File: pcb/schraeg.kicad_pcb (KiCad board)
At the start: 2 copper layers, 39.5 x 110 mm, 99 parts, among them J1 PJ398SM, J2 PJ398SM, J3 PJ398SM, J4 PJ398SM, J5 PJ398SM, J6 PJ398SM, J7 PJ398SM, J8 POWER, SW1 CS12ANW03, SW2 CS12ANW03, SW3 CS12ANW03, U1 TL074, U2 TL074, U3 V2164, U4 TL074, U5 TL074

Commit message: Panel design on kicad and iBOM updated.
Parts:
- added G***: LOGO, schraeg:silkF, F.Cu at (76.0, 105.0)
- added G***: LOGO, schraeg:copperF, F.Cu at (76.0, 105.0)
- added G***: LOGO, schraeg:maskF, F.Cu at (76.0, 105.0)
- added REF**: MountingHole_3.2mm_M3, MountingHole:MountingHole_3.2mm_M3, F.Cu at (99.5, 145.5)
- added REF**: MountingHole_3.2mm_M3, MountingHole:MountingHole_3.2mm_M3, F.Cu at (96.8, 145.5)
- added REF**: MountingHole_3.2mm_M3, MountingHole:MountingHole_3.2mm_M3, F.Cu at (99.5, 64.5)
- added REF**: MountingHole_3.2mm_M3, MountingHole:MountingHole_3.2mm_M3, F.Cu at (99.5, 63.5)
- added REF**: MountingHole_3.2mm_M3, MountingHole:MountingHole_3.2mm_M3, F.Cu at (99.5, 62.5)
- added REF**: MountingHole_3.2mm_M3, MountingHole:MountingHole_3.2mm_M3, F.Cu at (99.5, 61.5)
- added REF**: MountingHole_3.2mm_M3, MountingHole:MountingHole_3.2mm_M3, F.Cu at (99.5, 60.5)
- added REF**: MountingHole_3.2mm_M3, MountingHole:MountingHole_3.2mm_M3, F.Cu at (96.8, 64.5)
- added REF**: MountingHole_3.2mm_M3, MountingHole:MountingHole_3.2mm_M3, F.Cu at (96.8, 63.5)
- added REF**: MountingHole_3.2mm_M3, MountingHole:MountingHole_3.2mm_M3, F.Cu at (96.8, 62.5)
- added REF**: MountingHole_3.2mm_M3, MountingHole:MountingHole_3.2mm_M3, F.Cu at (96.8, 61.5)
- added REF**: MountingHole_3.2mm_M3, MountingHole:MountingHole_3.2mm_M3, F.Cu at (99.5, 146.5)
- added REF**: MountingHole_3.2mm_M3, MountingHole:MountingHole_3.2mm_M3, F.Cu at (88.8, 166.2)
- added REF**: MountingHole_3.2mm_M3, MountingHole:MountingHole_3.2mm_M3, F.Cu at (63.2, 166.2)
- added REF**: MountingHole_3.2mm_M3, MountingHole:MountingHole_3.2mm_M3, F.Cu at (88.8, 43.8)
- added REF**: MountingHole_3.2mm_M3, MountingHole:MountingHole_3.2mm_M3, F.Cu at (96.8, 60.5)
- added REF**: MountingHole_3.2mm_M3, MountingHole:MountingHole_3.2mm_M3, F.Cu at (63.2, 43.8)
- added REF**: MountingHole_3.2mm_M3, MountingHole:MountingHole_3.2mm_M3, F.Cu at (99.5, 147.5)
- added REF**: MountingHole_3.2mm_M3, MountingHole:MountingHole_3.2mm_M3, F.Cu at (99.5, 148.5)
- added REF**: MountingHole_3.2mm_M3, MountingHole:MountingHole_3.2mm_M3, F.Cu at (99.5, 149.5)
- added REF**: MountingHole_3.2mm_M3, MountingHole:MountingHole_3.2mm_M3, F.Cu at (96.8, 149.5)
- added REF**: MountingHole_3.2mm_M3, MountingHole:MountingHole_3.2mm_M3, F.Cu at (96.8, 148.5)
- added REF**: MountingHole_3.2mm_M3, MountingHole:MountingHole_3.2mm_M3, F.Cu at (96.8, 147.5)
- added REF**: MountingHole_3.2mm_M3, MountingHole:MountingHole_3.2mm_M3, F.Cu at (96.8, 146.5)
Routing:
- net GND: vias 7 -> 8
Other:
- board size 39.5 x 110 mm -> 83.8 x 128.5 mm

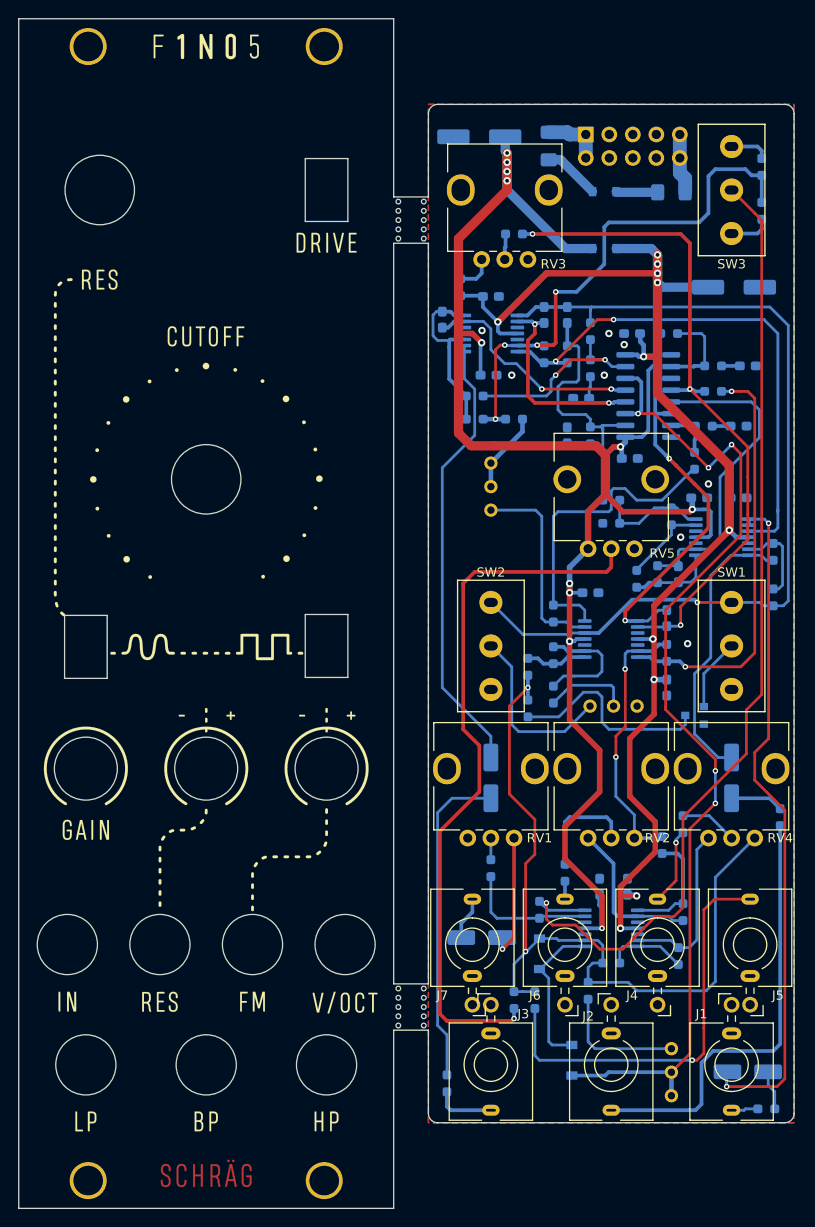
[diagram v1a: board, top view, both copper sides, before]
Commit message: Added silkscreen on PCB
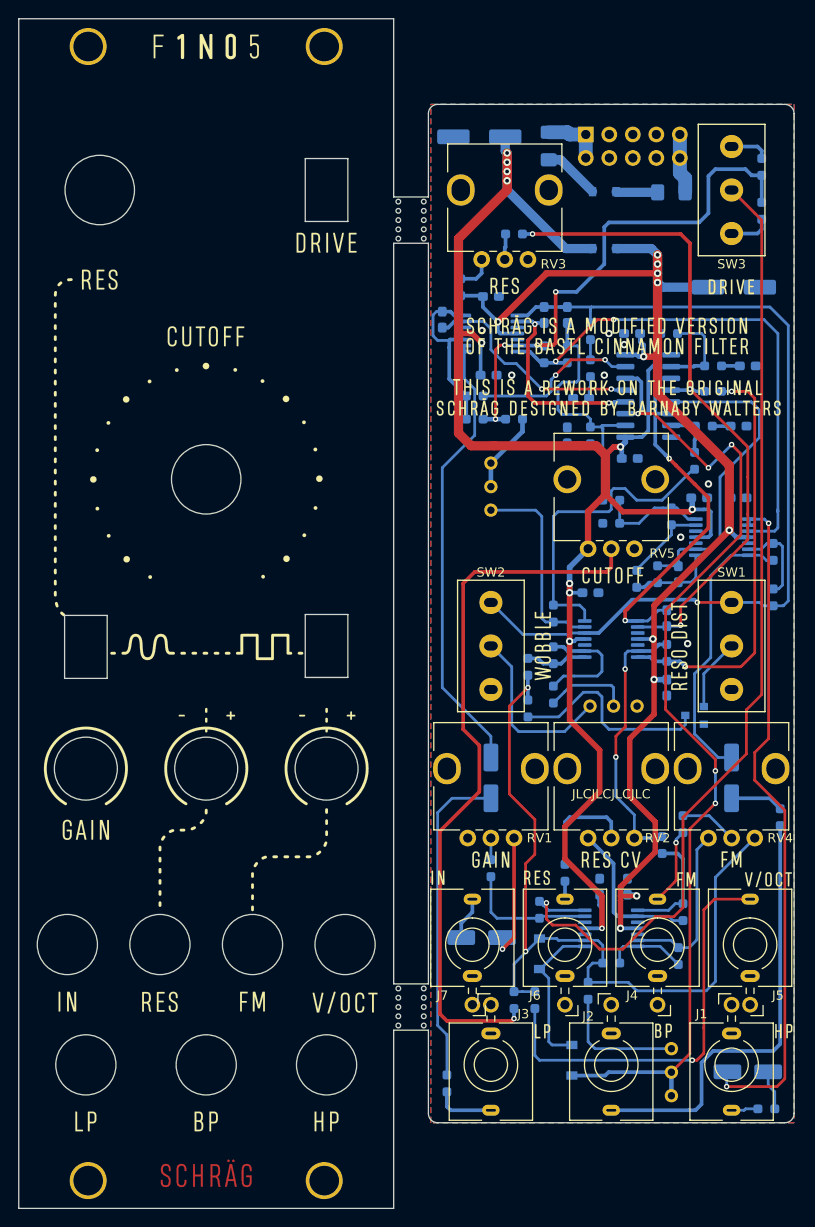
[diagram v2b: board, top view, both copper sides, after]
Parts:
- added G***: LOGO, schraeg:silkBoardB, B.Cu at (119.8, 105.0)
- added G***: LOGO, schraeg:silkBoardF, F.Cu at (119.8, 105.0)
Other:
- board text added: "JLCJLCJLCJLC"

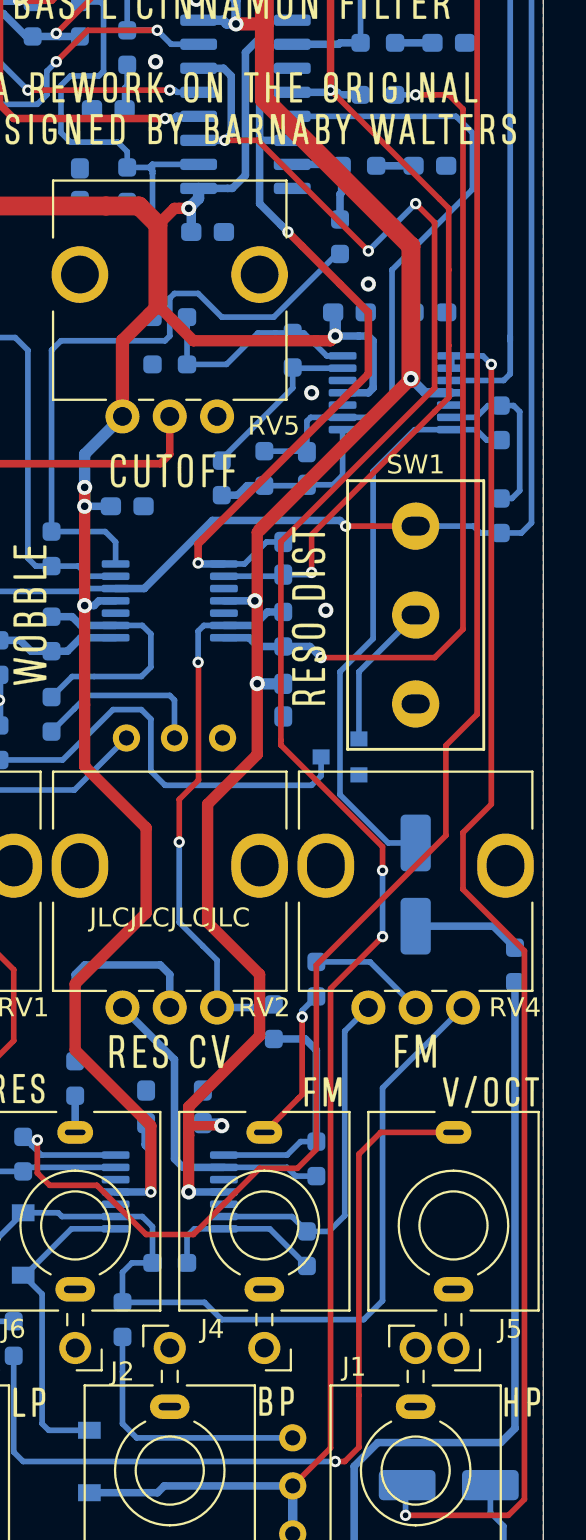
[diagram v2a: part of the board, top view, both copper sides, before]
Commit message: #8 - Added back the FM normalization. This time with a bit more than 1 OCT range.
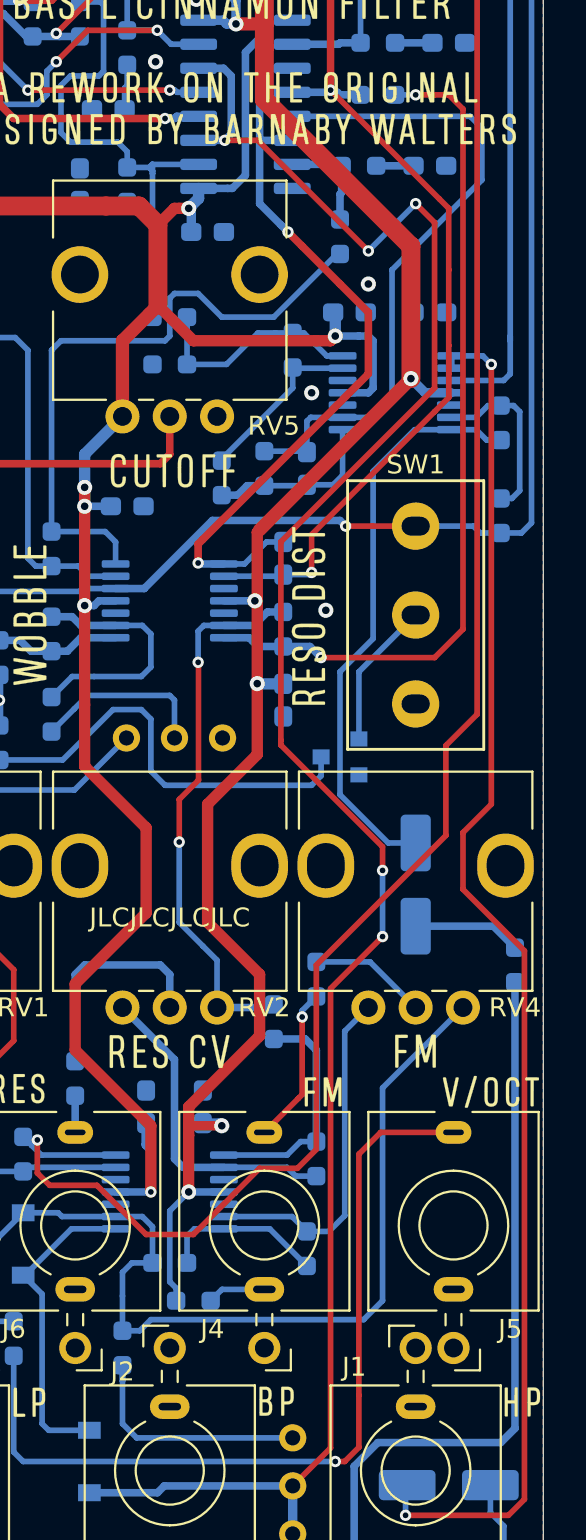
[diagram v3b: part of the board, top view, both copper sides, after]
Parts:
- added R11: 2M2, Resistor_SMD:R_0603_1608Metric_Pad0.98x0.95mm_HandSolder, B.Cu at (121.0, 144.8)
- moved R14 1.50 mm to (117.2, 147.2)
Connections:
- net AUDIO_IN renamed Net-(R21-Pad1)
- J4 pad TN: GND -> Net-(J4-PadTN)
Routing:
- net +12V: track 145.1 -> 151.4 mm
- net Net-(J4-PadTN): track 0.00 -> 3.09 mm
- net Net-(D1-Pad2): track 87.0 -> 88.4 mm
- net Net-(R14-Pad1): track 13.9 -> 12.9 mm
- net Net-(C9-Pad2): track 34.6 -> 35.4 mm

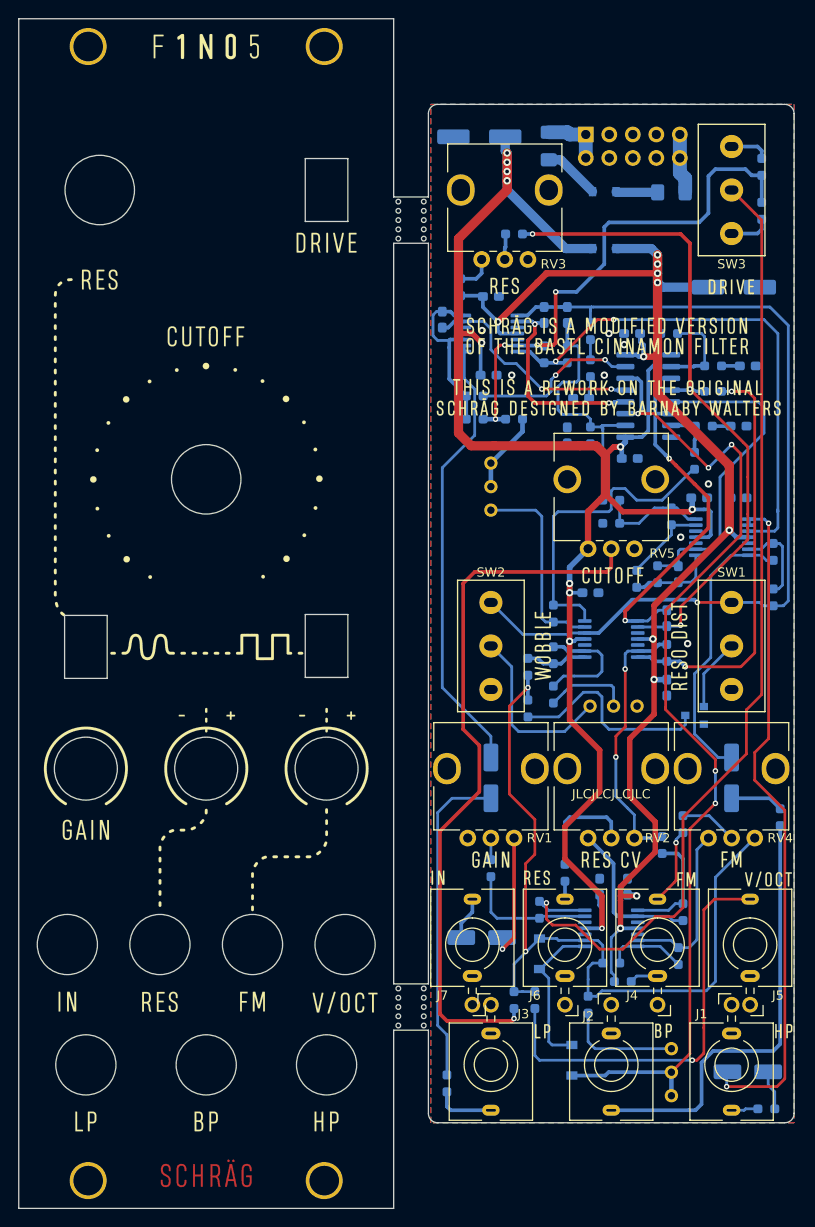
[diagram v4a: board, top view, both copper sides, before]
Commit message: #9 - Added LED input indicator.
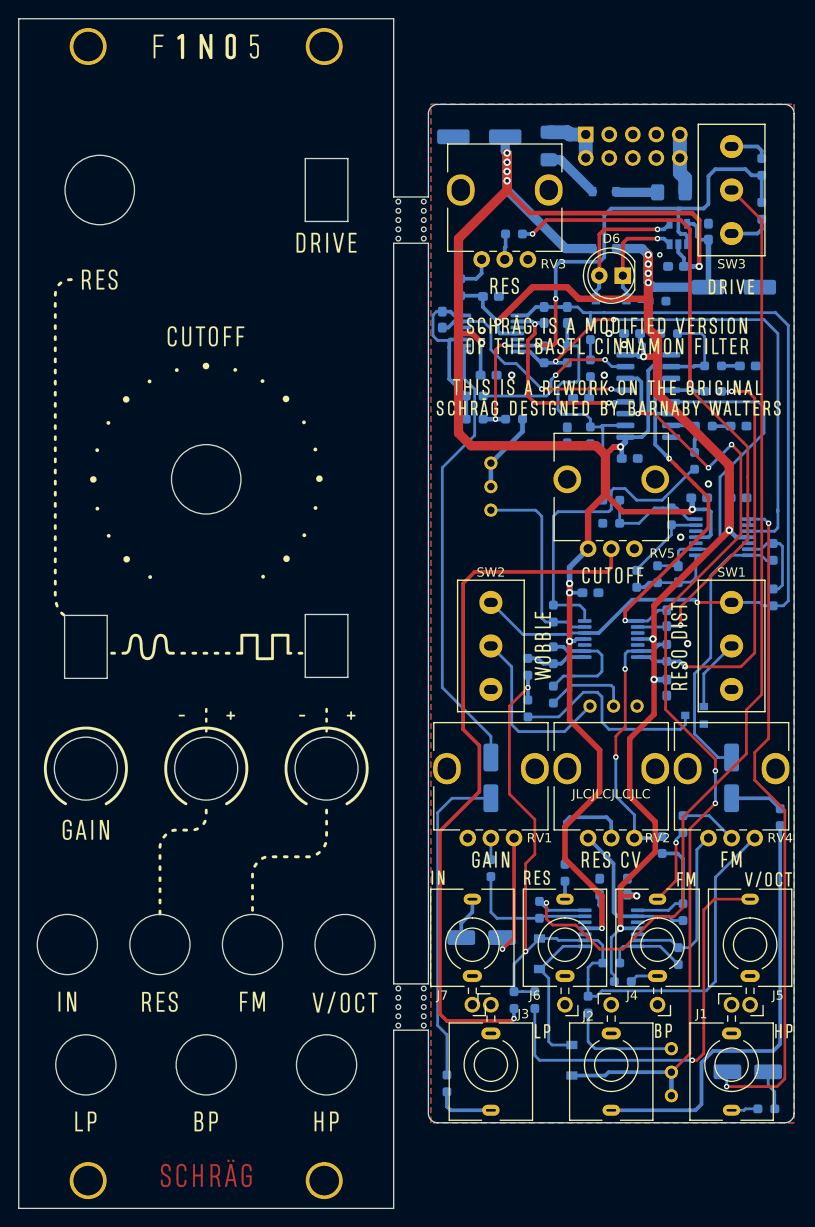
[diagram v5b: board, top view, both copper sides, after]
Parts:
- added C14: 100n, Capacitor_SMD:C_0603_1608Metric_Pad1.08x0.95mm_HandSolder, B.Cu at (130.2, 63.8)
- added C15: 100n, Capacitor_SMD:C_0603_1608Metric_Pad1.08x0.95mm_HandSolder, B.Cu at (126.8, 67.5)
- added D4: 1N4148, Diode_SMD:D_SOD-123, B.Cu at (119.8, 71.0)
- added D6: WP483IDT, LED_THT:LED_D5.0mm, F.Cu at (121.0, 68.5)
- added G***: LOGO, schraeg:maskB, B.Cu at (76.0, 105.0)
- added R44: 470R, Resistor_SMD:R_0603_1608Metric_Pad0.98x0.95mm_HandSolder, B.Cu at (124.8, 71.2)
- added U6: LM321, Package_TO_SOT_SMD:SOT-23-5, B.Cu at (127.0, 64.0)
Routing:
- net -12V: track 179.4 -> 211.4 mm, vias 11 -> 12
- net Net-(D4-Pad1): track 0.00 -> 15.2 mm, vias 0 -> 1
- net Net-(D4-Pad2): track 0.00 -> 14.2 mm, vias 0 -> 1
- net +12V: track 151.4 -> 159.4 mm
- net Net-(R21-Pad1): track 58.7 -> 64.6 mm
- net Net-(C3-Pad2): track 73.9 -> 76.0 mm
- net BP_OUT: track 97.6 -> 96.9 mm
- net GND: vias 8 -> 9

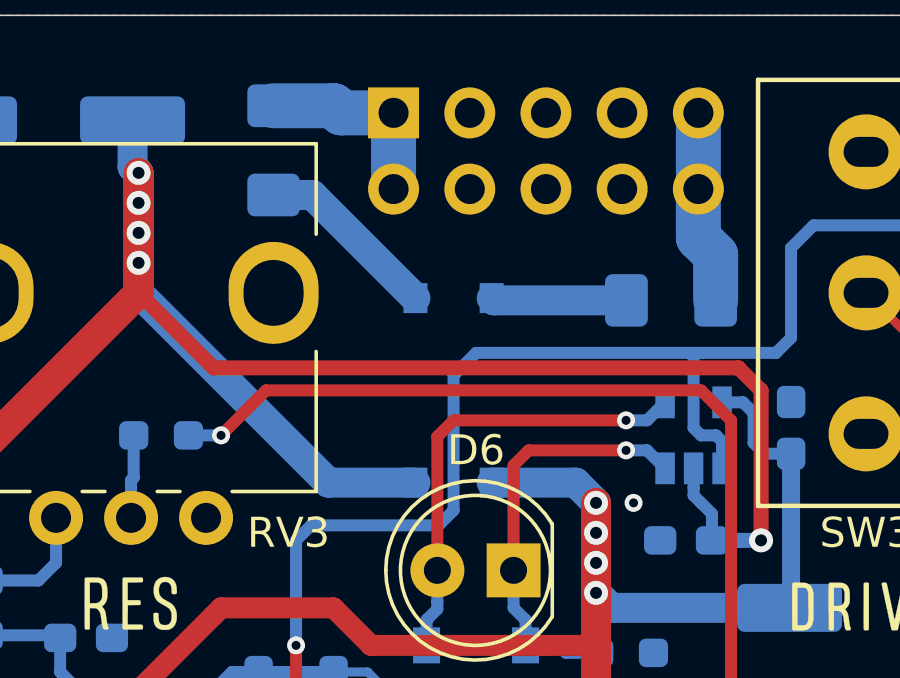
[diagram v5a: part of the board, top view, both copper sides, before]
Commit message: #10 - Corrected rectifier orientation.
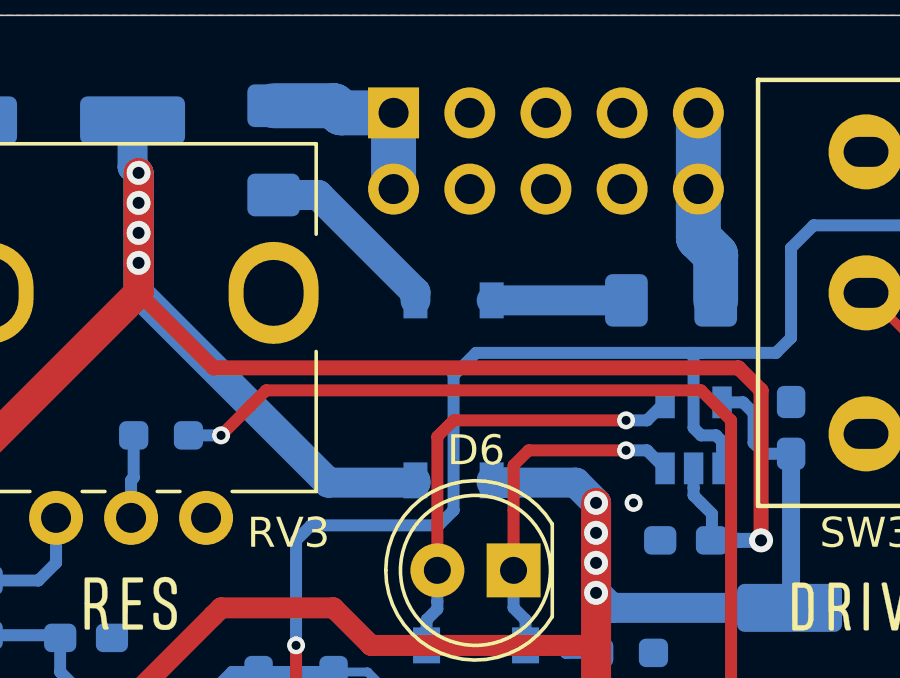
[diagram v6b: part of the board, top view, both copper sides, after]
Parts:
- D5: value MB2S -> MB1S; footprint Package_TO_SOT_SMD:TO-269AA -> Package_SO:SO-4_4.4x4.3mm_P2.54mm
- turned D5 to 90 degrees
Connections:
- D5 pad 1: Net-(D5-Pad1) -> +12V
- D5 pad 2: Net-(D5-Pad2) -> -12V
- D5 pad 3: +12V -> Net-(D5-Pad3)
- D5 pad 4: -12V -> Net-(D5-Pad4)
- F1 pad 1: Net-(D5-Pad1) -> Net-(D5-Pad3)
- F2 pad 1: Net-(D5-Pad2) -> Net-(D5-Pad4)
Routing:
- net Net-(D5-Pad3): track 0.00 -> 6.34 mm
- net Net-(D5-Pad1): track 6.15 -> 0.00 mm
- net Net-(D5-Pad2): track 4.52 -> 0.00 mm
- net Net-(D5-Pad4): track 0.00 -> 4.49 mm
- net +12V: track 159.4 -> 160.3 mm

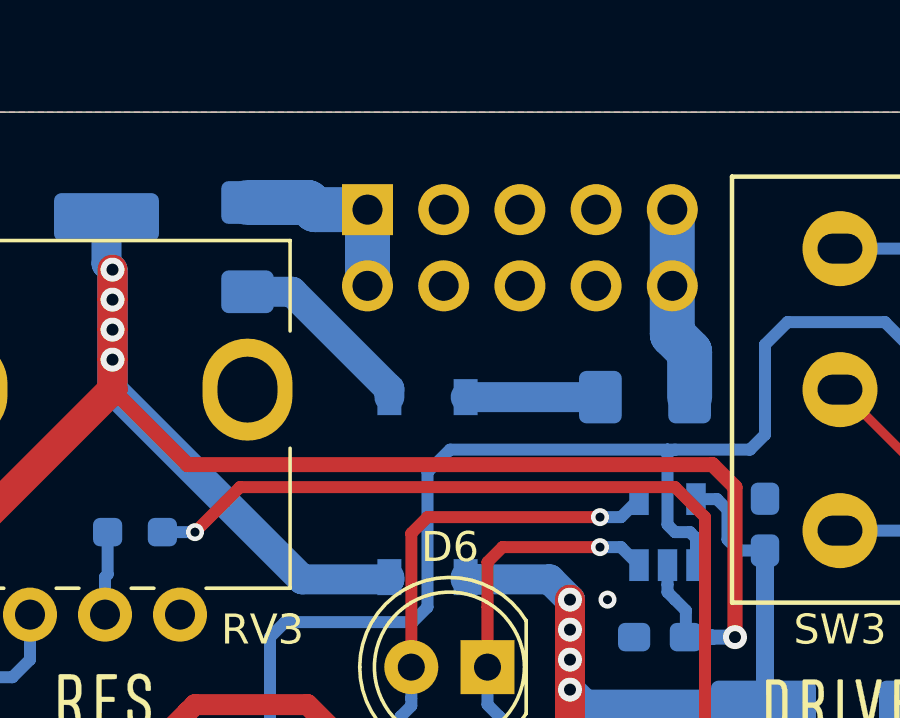
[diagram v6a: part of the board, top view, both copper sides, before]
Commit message: Corrected PTC footprint. From 1206 to 0805
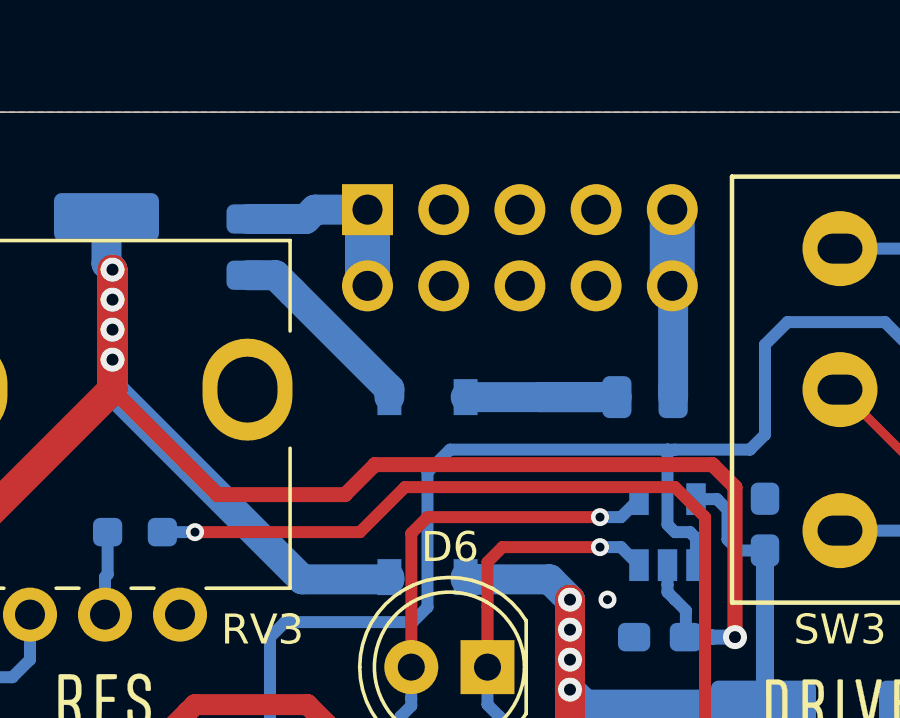
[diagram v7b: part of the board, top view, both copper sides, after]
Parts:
- F1, F2: footprint Fuse:Fuse_1206_3216Metric_Pad1.42x1.75mm_HandSolder -> Fuse:Fuse_0805_2012Metric
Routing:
- net Net-(D5-Pad4): track 4.49 -> 7.06 mm
- net -12V: track 211.5 -> 212.3 mm
